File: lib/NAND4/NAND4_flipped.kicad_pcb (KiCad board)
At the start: 2 copper layers, 8 parts

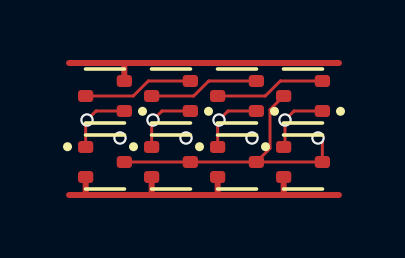
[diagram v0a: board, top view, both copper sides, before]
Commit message: All cells now use 1mm*4mm grid rather than 1.1mm*4.4mm
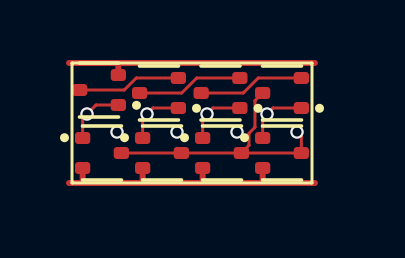
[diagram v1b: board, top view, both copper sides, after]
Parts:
- moved P4 0.76 mm to (7.00, 3.00)
- moved N4 0.71 mm to (7.00, 1.00)
- moved P3 0.58 mm to (5.00, 3.00)
- moved N3 0.56 mm to (4.95, 1.00)
- moved P2 0.42 mm to (3.00, 3.00)
- moved N2 0.41 mm to (2.90, 1.00)
- moved P1 0.32 mm to (1.00, 3.00)
- moved N1 0.28 mm to (0.90, 0.90)
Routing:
- net VDD: track 11.4 -> 10.3 mm
- net GND: track 9.62 -> 8.62 mm
- net Y: track 10.0 -> 9.05 mm

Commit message: Make the pads of my SOT523 footprint very slightly smaller, which is enough to route all the cells and leave the mosfets exactly on the grid
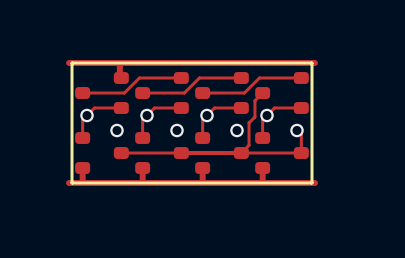
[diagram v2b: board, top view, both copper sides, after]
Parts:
- N1, N2, N3, N4, P1, P2, P3, P4: footprint Package_TO_SOT_SMD:SOT-523 -> RV523:SOT523
- moved N1 0.14 mm to (1.00, 1.00)
- moved N2 0.10 mm to (3.00, 1.00)
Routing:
- net Y: track 9.05 -> 11.1 mm

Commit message: Propagate MOSFET values to the cells' PCBs
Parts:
- N1, N2, N3, N4: value (none) -> NMOS
- P1, P2, P3, P4: value (none) -> PMOS
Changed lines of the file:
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@@
 			)
 		)
-		(property "Value" ""
+		(property "Value" "PMOS"
 			(at 0 0 0)
 			(layer "F.Fab")
@@
 			)
 		)
-		(property "Value" ""
+		(property "Value" "PMOS"
 			(at 0 0 0)
 			(layer "F.Fab")
@@
 			)
 		)
-		(property "Value" ""
+		(property "Value" "PMOS"
 			(at 0 0 0)
 			(layer "F.Fab")
@@
 			)
 		)
-		(property "Value" ""
+		(property "Value" "NMOS"
 			(at 0 0 180)
 			(layer "F.Fab")
@@
 			)
 		)
-		(property "Value" ""
+		(property "Value" "PMOS"
 			(at 0 0 0)
 			(layer "F.Fab")
@@
 			)
 		)
-		(property "Value" ""
+		(property "Value" "NMOS"
 			(at 0 0 180)
 			(layer "F.Fab")
@@
 			)
 		)
-		(property "Value" ""
+		(property "Value" "NMOS"
 			(at 0 0 180)
 			(layer "F.Fab")
@@
 			)
 		)
-		(property "Value" ""
-			(at 0 0 180)
-			(layer "F.Fab")
+		(property "Value" "NMOS"
+			(at 0 0 180)
+			(layer "F.Fab")
